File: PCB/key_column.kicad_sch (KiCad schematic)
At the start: 4 parts, among them SW1 SW_Push

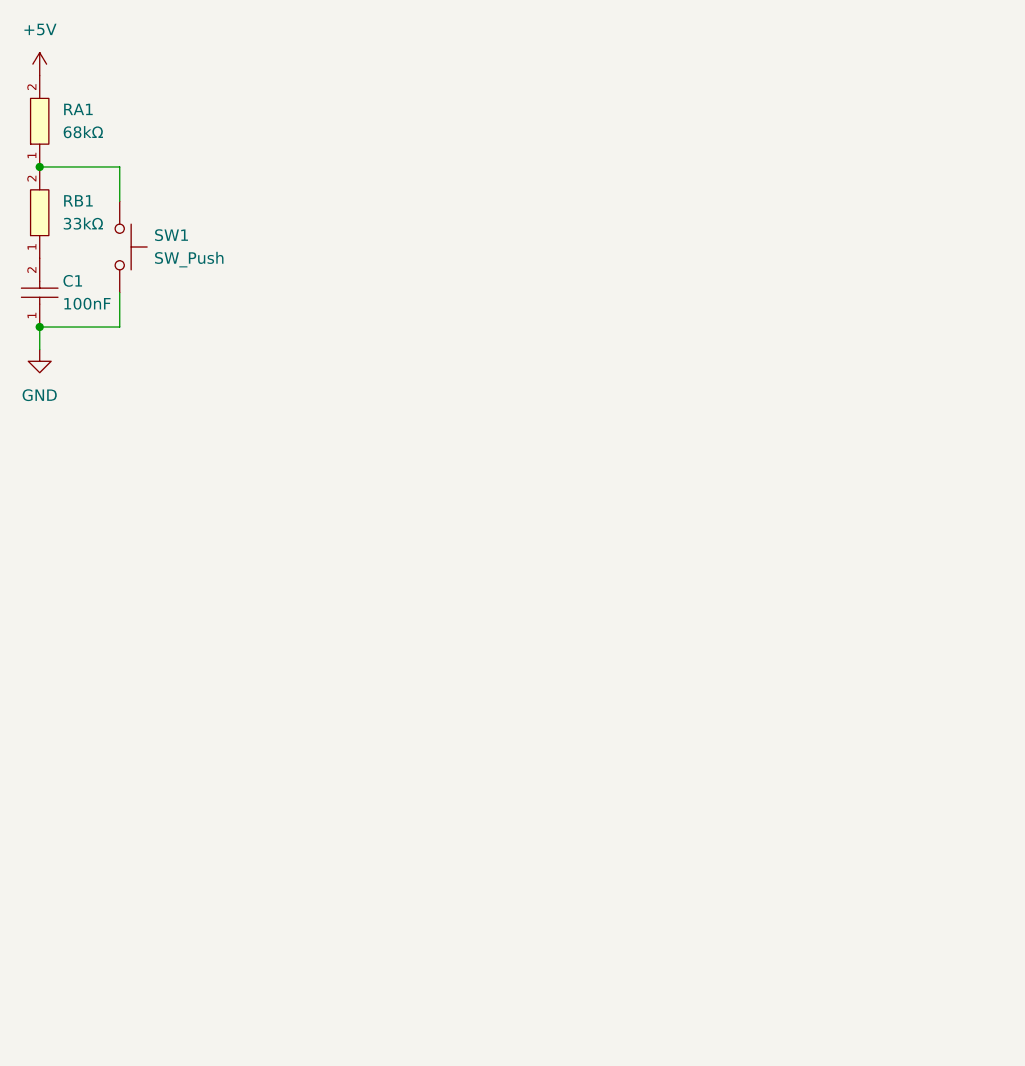
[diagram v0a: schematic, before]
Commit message: Figured out the layout, now working on the PCB for each half.
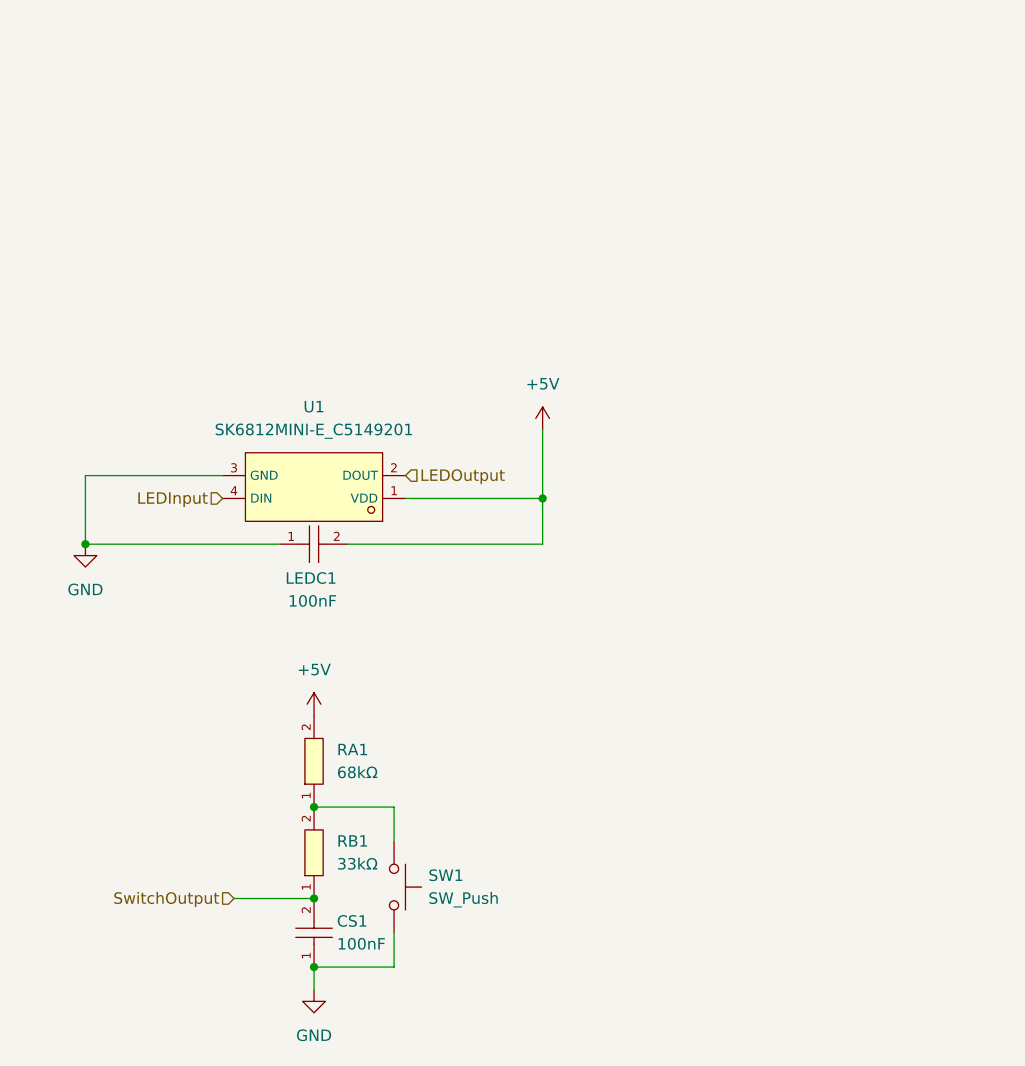
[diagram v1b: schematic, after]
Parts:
- added LEDC1: 100nF, Package_SO:SOIC-16_3.9x9.9mm_P1.27mm, symbol JLCPCB:CL05B104KO5NNNC
- added U1: SK6812MINI-E_C5149201, footprint:LED-SMD_L3.2-W2.8-TR, symbol JLCPCB:SK6812MINI-E_C5149201
- SW1: footprint (none) -> PCM_Switch_Keyboard_Hotswap_Kailh:SW_Hotswap_Kailh_MX; symbol Switch:SW_Push -> JLCPCB:Keyswitch; LCSC (none) -> C5184526
- renumbered C1 to CS1
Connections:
- net +5V: now also LEDC1.2, U1.1 (VDD)
- net GND: now also LEDC1.1, U1.3 (GND)
- net SwitchOutput: now reaches CS1.2, RB1.1
- new net LEDInput: U1.4 (DIN)
- new net LEDOutput: U1.2 (DOUT)
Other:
- moved on the sheet: CS1, RA1, RB1, SW1

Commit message: Working on STM32 circuit
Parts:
- CS1: footprint footprint:C0402 -> Capacitor_SMD:C_0402_1005Metric
- LEDC1: footprint Package_SO:SOIC-16_3.9x9.9mm_P1.27mm -> Capacitor_SMD:C_0402_1005Metric

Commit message: Plugin works.
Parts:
- renumbered LEDC1 to CL1201, CS1 to CS1201, RA1 to RA1201, RB1 to RB1201, SW1 to SW1201, U1 to U1201

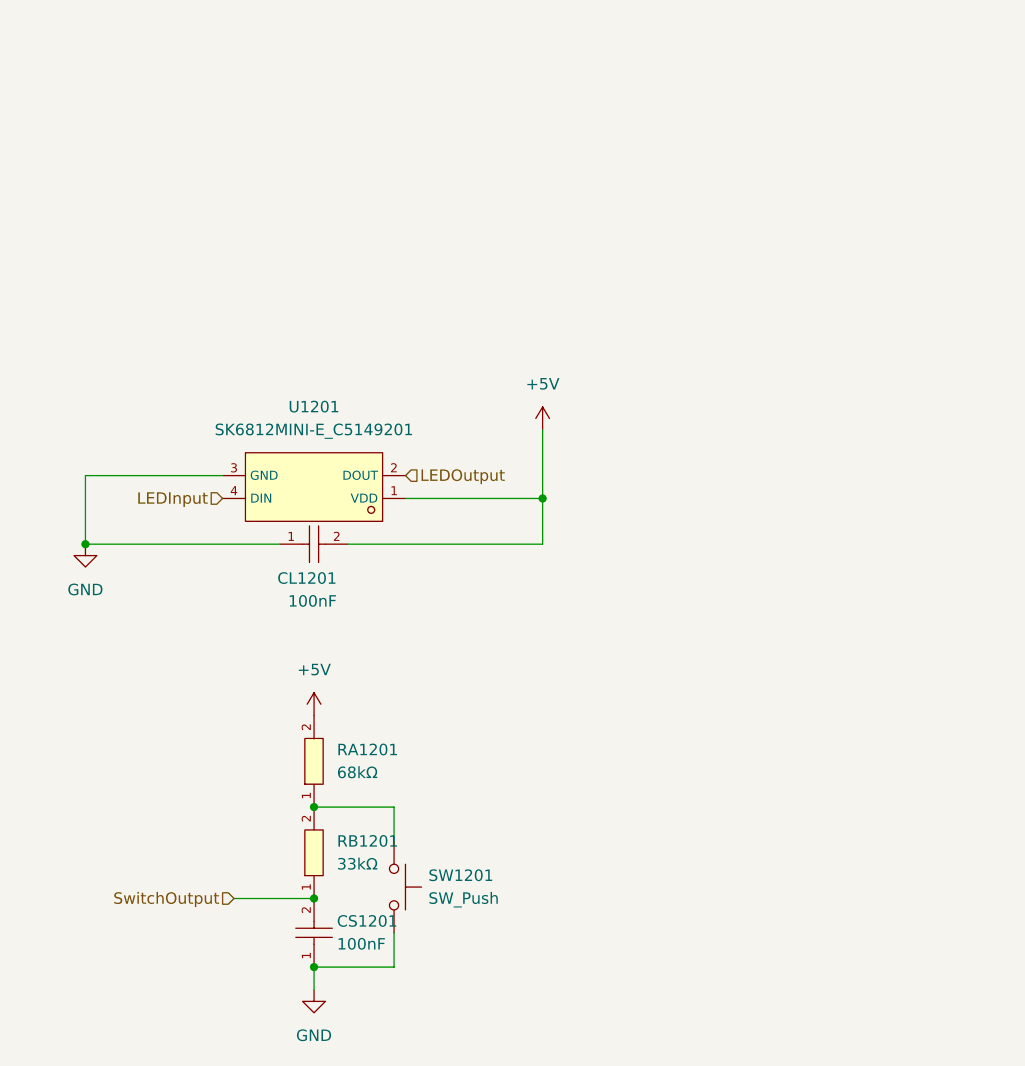
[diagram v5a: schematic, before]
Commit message: Updated schematics for KiCAD 8
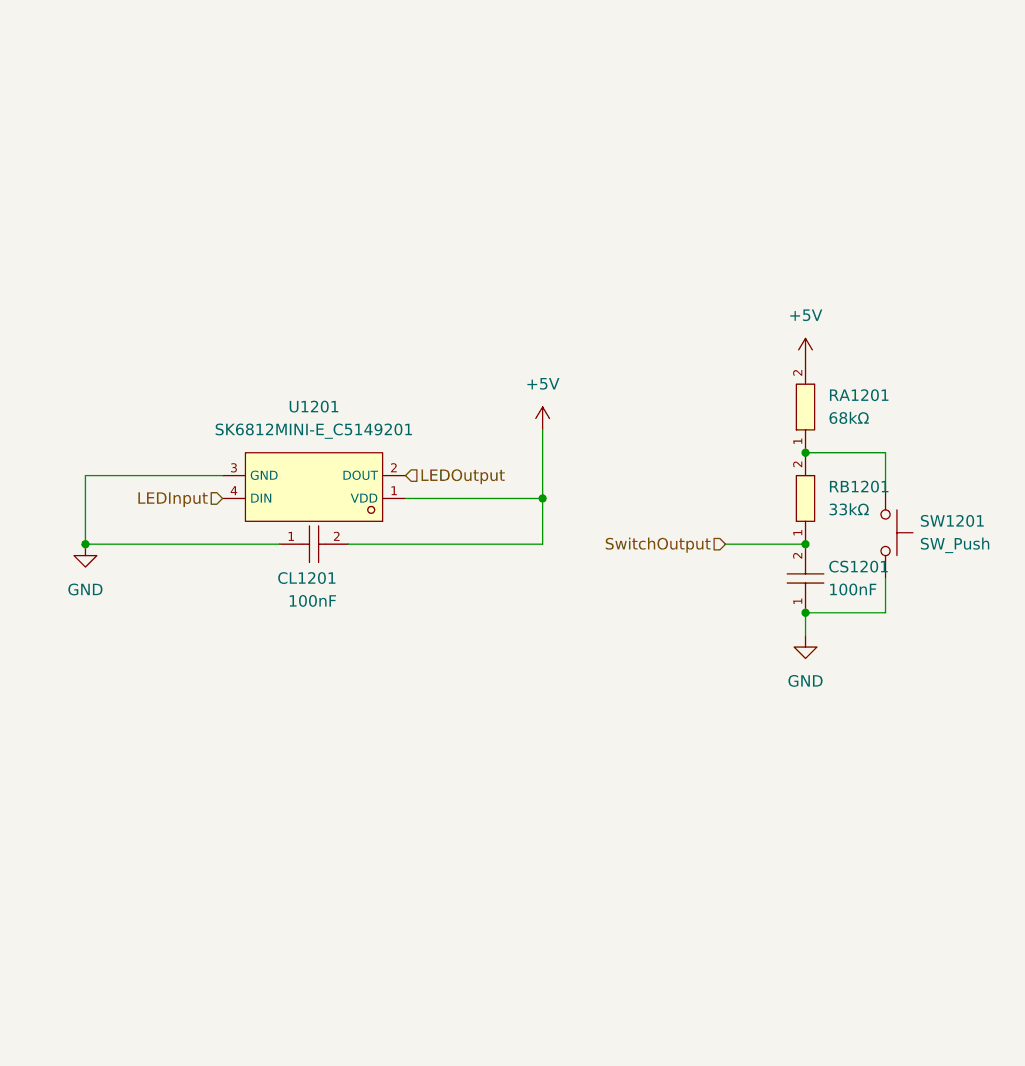
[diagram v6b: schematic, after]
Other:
- moved on the sheet: CS1201, RA1201, RB1201, SW1201
